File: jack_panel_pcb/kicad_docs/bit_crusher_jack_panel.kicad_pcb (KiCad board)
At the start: 2 copper layers, 81.3 x 25.4 mm, 0 parts

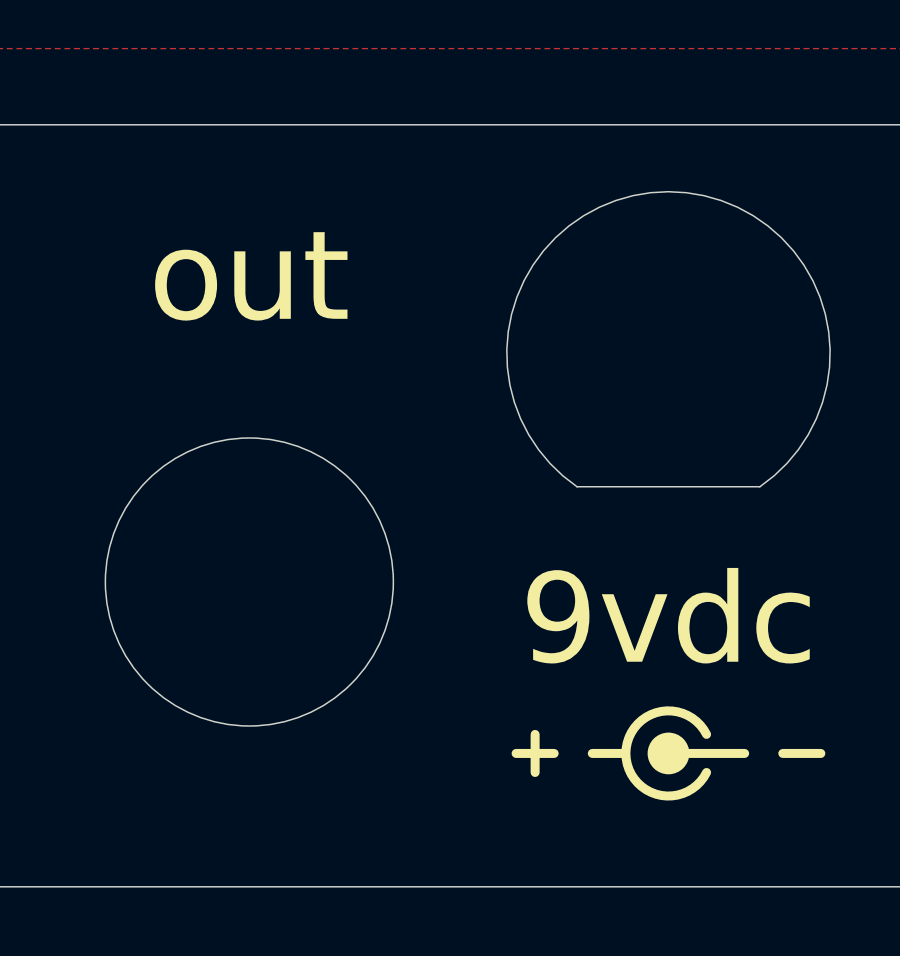
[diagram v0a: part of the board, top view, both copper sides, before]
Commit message: fix jack panel issue where front mask was missing
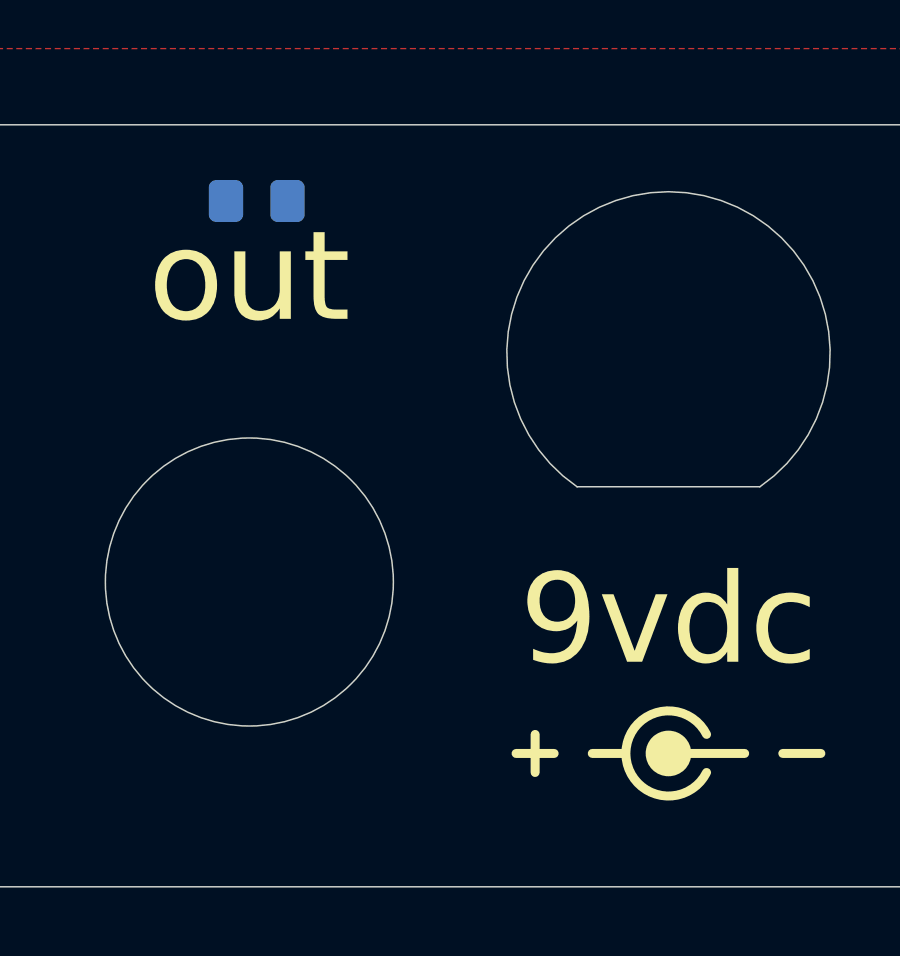
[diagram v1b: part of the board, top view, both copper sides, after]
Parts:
- added R1: R, Resistor_SMD:R_0805_2012Metric_Pad1.15x1.40mm_HandSolder, B.Cu at (103.1, 38.1)
- added TP1: TestPoint, TestPoint:TestPoint_Pad_D1.0mm, F.Cu at (116.8, 56.5)
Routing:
- net GND: vias 0 -> 1
- added copper zone on B.Cu, net GND
- added copper zone on F.Cu, net GND
- removed copper zone on B.Cu, net (none)
- removed copper zone on F.Cu, net (none)
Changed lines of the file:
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@@
     (thickness 1.6)
     (drawings 42)
-    (tracks 0)
+    (tracks 1)
     (zones 0)
-    (modules 0)
-    (nets 1)
+    (modules 2)
+    (nets 2)
   )
   (page A4)
   (layers
-    (0 F.Cu signal)
-    (31 B.Cu signal)
+    (0 F.Cu signal hide)
+    (31 B.Cu signal hide)
     (32 B.Adhes user)
     (33 F.Adhes user)
@@
     (mod_text_size 1 1)
     (mod_text_width 0.15)
-    (pad_size 2.72 3.24)
-    (pad_drill 1.1)
+    (pad_size 1 1)
+    (pad_drill 0)
     (pad_to_mask_clearance 0.05)
     (aux_axis_origin 0 0)
@@
       (layerselection 0x010f0_ffffffff)
       (usegerberextensions false)
-      (usegerberattributes true)
-      (usegerberadvancedattributes true)
+      (usegerberattributes false)
+      (usegerberadvancedattributes false)
       (creategerberjobfile false)
       (excludeedgelayer true)
@@
   )
   (net 0 "")
+  (net 1 GND)
   (net_class Default "This is the default net class."
     (clearance 0.2)
@@
     (uvia_dia 0.3)
     (uvia_drill 0.1)
+    (add_net GND)
+  )
+  (module TestPoint:TestPoint_Pad_D1.0mm (layer F.Cu)
+    (at 116.84 56.515)
+    (descr "SMD pad as test Point, diameter 1.0mm")
+    (tags "test point SMD pad")
+    (attr virtual)
+    (fp_text reference TP1 (at 0 -1.448) (layer F.SilkS) hide
+      (effects (font (size 1 1) (thickness 0.15)))
+    )
+    (fp_text value TestPoint (at 0 1.55) (layer F.Fab)
+      (effects (font (size 1 1) (thickness 0.15)))
+    )
+    (fp_text user %R (at 0 -1.45) (layer F.Fab)
+      (effects (font (size 1 1) (thickness 0.15)))
+    )
+    (fp_circle (center 0 0) (end 1 0) (layer F.CrtYd) (width 0.05))
+    (fp_circle (center 0 0) (end 0 0.7) (layer F.SilkS) (width 0.12))
+    (pad 1 smd circle (at 0 0) (size 1 1) (layers F.Cu F.Mask)
+      (net 1 GND))
+  )
+  (module Resistor_SMD:R_0805_2012Metric_Pad1.15x1.40mm_HandSolder (layer B.Cu)
+    (at 103.115 38.1)
+    (descr "Resistor SMD 0805 (2012 Metric), square (rectangular) end terminal, IPC_7351 nominal with elongated pad for handsoldering. (Body size source: https://docs.google.com/spreadsheets/d/1BsfQQcO9C6DZCsRaXUlFlo91Tg2WpOkGARC1WS5S8t0/edit?usp=sharing), generated with kicad-footprint-generator")
+    (tags "resistor handsolder")
+    (attr smd)
+    (fp_text reference R1 (at 0 1.65) (layer B.SilkS) hide
+      (effects (font (size 1 1) (thickness 0.15)) (justify mirror))
+    )
+    (fp_text value R (at 0 -1.65) (layer B.Fab)
+      (effects (font (size 1 1) (thickness 0.15)) (justify mirror))
+    )
+    (fp_line (start -1 -0.6) (end -1 0.6) (layer B.Fab) (width 0.1))
+    (fp_line (start -1 0.6) (end 1 0.6) (layer B.Fab) (width 0.1))
+    (fp_line (start 1 0.6) (end 1 -0.6) (layer B.Fab) (width 0.1))
+    (fp_line (start 1 -0.6) (end -1 -0.6) (layer B.Fab) (width 0.1))
+    (fp_line (start -0.261252 0.71) (end 0.261252 0.71) (layer B.SilkS) (width 0.12))
+    (fp_line (start -0.261252 -0.71) (end 0.261252 -0.71) (layer B.SilkS) (width 0.12))
+    (fp_line (start -1.85 -0.95) (end -1.85 0.95) (layer B.CrtYd) (width 0.05))
+    (fp_line (start -1.85 0.95) (end 1.85 0.95) (layer B.CrtYd) (width 0.05))
+    (fp_line (start 1.85 0.95) (end 1.85 -0.95) (layer B.CrtYd) (width 0.05))
+    (fp_line (start 1.85 -0.95) (end -1.85 -0.95) (layer B.CrtYd) (width 0.05))
+    (fp_text user %R (at 0 0) (layer B.Fab)
+      (effects (font (size 0.5 0.5) (thickness 0.08)) (justify mirror))
+    )
+    (pad 2 smd roundrect (at 1.025 0) (size 1.15 1.4) (layers B.Cu B.Paste B.Mask) (roundrect_rratio 0.217391)
+      (net 1 GND))
+    (pad 1 smd roundrect (at -1.025 0) (size 1.15 1.4) (layers B.Cu B.Paste B.Mask) (roundrect_rratio 0.217391)
+      (net 1 GND))
+    (model ${KISYS3DMOD}/Resistor_SMD.3dshapes/R_0805_2012Metric.wrl
+      (at (xyz 0 0 0))
+      (scale (xyz 1 1 1))
+      (rotate (xyz 0 0 0))
+    )
   )
   (gr_arc (start 116.84 43.18) (end 119.887999 47.624999) (angle -291.1220214) (layer Edge.Cuts) (width 0.05))
@@
   (gr_line (start 81.28 60.96) (end 152.4 60.96) (layer Edge.Cuts) (width 0.05))
   (gr_line (start 76.2 40.64) (end 76.2 55.88) (layer Edge.Cuts) (width 0.05))
-  (zone (net 0) (net_name "") (layer F.Cu) (hatch edge 0.508)
+  (via (at 116.84 56.515) (size 0.8) (drill 0.4) (layers F.Cu B.Cu) (net 1))
+  (zone (net 1) (net_name GND) (layer F.Cu) (hatch edge 0.508)
     (connect_pads (clearance 0.508))
     (min_thickness 0.254)
@@
     )
   )
-  (zone (net 0) (net_name "") (layer B.Cu) (hatch edge 0.508)
+  (zone (net 1) (net_name GND) (layer B.Cu) (hatch edge 0.508)
     (connect_pads (clearance 0.508))
     (min_thickness 0.254)
